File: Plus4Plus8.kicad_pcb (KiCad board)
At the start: 2 copper layers, 22 parts, among them CN1 JOY1, CN2 JOY2, CN3 JOY3, CN4 JOY4, CN5 JOY5, CN6 JOY6, CN7 JOY7, CN8 JOY8, CN9 PLUS4_USERPORT, U1 CD4051B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

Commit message: Initial layout
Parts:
- moved CN1 54.4 mm to (130.9, 121.8)
- moved CN2 54.4 mm to (130.6, 88.8)
- moved CN3 54.4 mm to (129.8, 58.3)
- moved CN4 54.4 mm to (143.4, 31.5)
- moved CN5 54.4 mm to (175.0, 31.0)
- moved CN6 54.4 mm to (188.6, 59.2)
- moved CN7 54.4 mm to (188.6, 91.1)
- moved CN9 54.4 mm to (158.2, 149.1)
- moved RN2 54.4 mm to (144.5, 95.9)
- moved RN3 54.4 mm to (144.1, 66.8)
- moved RN6 54.4 mm to (175.1, 65.9)
- moved U1 54.4 mm to (150.9, 59.9)
- moved U2 54.4 mm to (150.6, 79.0)
- moved U4 54.4 mm to (151.3, 113.7)
- moved U5 54.4 mm to (150.6, 130.7)
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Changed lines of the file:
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@@
   )
   (module Plus4Plus8:DB_9M (layer F.Cu)
-    (at 86.995 89.789 270)
+    (at 130.937 121.793 270)
     (descr "D-SUB 9 pin plug, Tyco P/N 4-338168-2")
     (fp_text reference CN1 (at 0 -2.7 90) (layer F.SilkS)
@@
   )
   (module Plus4Plus8:DB_9M (layer F.Cu)
-    (at 86.614 56.769 270)
+    (at 130.556 88.773 270)
     (descr "D-SUB 9 pin plug, Tyco P/N 4-338168-2")
     (fp_text reference CN2 (at 0 -2.7 90) (layer F.SilkS)
@@
   )
   (module Plus4Plus8:DB_9M (layer F.Cu)
-    (at 85.852 26.289 270)
+    (at 129.794 58.293 270)
     (descr "D-SUB 9 pin plug, Tyco P/N 4-338168-2")
     (fp_text reference CN3 (at 0 -2.7 90) (layer F.SilkS)
@@
   )
   (module Plus4Plus8:DB_9M (layer F.Cu)
-    (at 99.441 -0.508 180)
+    (at 143.383 31.496 180)
     (descr "D-SUB 9 pin plug, Tyco P/N 4-338168-2")
     (fp_text reference CN4 (at 0 -2.7) (layer F.SilkS)
@@
   )
   (module Plus4Plus8:DB_9M (layer F.Cu)
-    (at 131.064 -1.016 180)
+    (at 175.006 30.988 180)
     (descr "D-SUB 9 pin plug, Tyco P/N 4-338168-2")
     (fp_text reference CN5 (at 0 -2.7) (layer F.SilkS)
@@
   )
   (module Plus4Plus8:DB_9M (layer F.Cu)
-    (at 144.653 27.178 90)
+    (at 188.595 59.182 90)
     (descr "D-SUB 9 pin plug, Tyco P/N 4-338168-2")
     (fp_text reference CN6 (at 0 -2.7 90) (layer F.SilkS)
@@
   )
   (module Plus4Plus8:DB_9M (layer F.Cu)
-    (at 144.653 59.055 90)
+    (at 188.595 91.059 90)
     (descr "D-SUB 9 pin plug, Tyco P/N 4-338168-2")
     (fp_text reference CN7 (at 0 -2.7 90) (layer F.SilkS)
@@
   )
   (module Plus4Plus8:DB_9M (layer F.Cu)
-    (at 144.145 91.948 90)
+    (at 188.087 123.952 90)
     (descr "D-SUB 9 pin plug, Tyco P/N 4-338168-2")
     (fp_text reference CN8 (at 0 -2.7 90) (layer F.SilkS)
@@
   )
   (module Plus4Plus8:PLUS4_USERPORT (layer F.Cu)
-    (at 114.3 117.094)
+    (at 158.242 149.098)
     (attr smd)
     (fp_text reference CN9 (at 25.74 -2) (layer F.SilkS)
@@
   )
   (module Resistor_THT:R_Array_SIP6 (layer F.Cu)
-    (at 100.711 95.758 90)
+    (at 144.653 127.762 90)
     (descr "6-pin Resistor SIP pack")
     (tags R)
@@
   )
   (module Resistor_THT:R_Array_SIP6 (layer F.Cu)
-    (at 100.584 63.881 90)
+    (at 144.526 95.885 90)
     (descr "6-pin Resistor SIP pack")
     (tags R)
@@
   )
   (module Resistor_THT:R_Array_SIP6 (layer F.Cu)
-    (at 100.203 34.798 90)
+    (at 144.145 66.802 90)
     (descr "6-pin Resistor SIP pack")
     (tags R)
@@
   )
   (module Resistor_THT:R_Array_SIP6 (layer F.Cu)
-    (at 111.633 12.192 180)
+    (at 155.575 44.196 180)
     (descr "6-pin Resistor SIP pack")
     (tags R)
@@
   )
   (module Resistor_THT:R_Array_SIP6 (layer F.Cu)
-    (at 131.318 12.065 180)
+    (at 175.26 44.069 180)
     (descr "6-pin Resistor SIP pack")
     (tags R)
@@
   )
   (module Resistor_THT:R_Array_SIP6 (layer F.Cu)
-    (at 131.191 33.909 90)
+    (at 175.133 65.913 90)
     (descr "6-pin Resistor SIP pack")
     (tags R)
@@
   )
   (module Resistor_THT:R_Array_SIP6 (layer F.Cu)
-    (at 130.937 65.024 90)
+    (at 174.879 97.028 90)
     (descr "6-pin Resistor SIP pack")
     (tags R)
@@
   )
   (module Resistor_THT:R_Array_SIP6 (layer F.Cu)
-    (at 130.556 98.171 90)
+    (at 174.498 130.175 90)
     (descr "6-pin Resistor SIP pack")
     (tags R)
@@
   )
   (module Package_DIP:DIP-16_W7.62mm_LongPads (layer F.Cu)
-    (at 106.934 27.94 90)
+    (at 150.876 59.944 90)
     (descr "16-lead though-hole mounted DIP package, row spacing 7.62 mm (300 mils), LongPads")
     (tags "THT DIP DIL PDIP 2.54mm 7.62mm 300mil LongPads")
@@
   )
   (module Package_DIP:DIP-16_W7.62mm_LongPads (layer F.Cu)
-    (at 106.68 46.99 90)
+    (at 150.622 78.994 90)
     (descr "16-lead though-hole mounted DIP package, row spacing 7.62 mm (300 mils), LongPads")
     (tags "THT DIP DIL PDIP 2.54mm 7.62mm 300mil LongPads")
@@
   )
   (module Package_DIP:DIP-16_W7.62mm_LongPads (layer F.Cu)
-    (at 107.188 64.643 90)
+    (at 151.13 96.647 90)
     (descr "16-lead though-hole mounted DIP package, row spacing 7.62 mm (300 mils), LongPads")
     (tags "THT DIP DIL PDIP 2.54mm 7.62mm 300mil LongPads")
@@
   )
   (module Package_DIP:DIP-16_W7.62mm_LongPads (layer F.Cu)
-    (at 107.315 81.661 90)
+    (at 151.257 113.665 90)
     (descr "16-lead though-hole mounted DIP package, row spacing 7.62 mm (300 mils), LongPads")
     (tags "THT DIP DIL PDIP 2.54mm 7.62mm 300mil LongPads")
@@
   )
   (module Package_DIP:DIP-16_W7.62mm_LongPads (layer F.Cu)
-    (at 106.68 98.679 90)
+    (at 150.622 130.683 90)
     (descr "16-lead though-hole mounted DIP package, row spacing 7.62 mm (300 mils), LongPads")
     (tags "THT DIP DIL PDIP 2.54mm 7.62mm 300mil LongPads")

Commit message: New layout, way funnier
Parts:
- CN1, CN2, CN3, CN4, CN5, CN6, CN7, CN8: footprint Plus4Plus8:DB_9M -> Connector_Dsub:DSUB-9_Male_EdgeMount_P2.77mm
- CN9: value PLUS4_USERPORT -> DB15F; footprint Plus4Plus8:PLUS4_USERPORT -> Connector_Dsub:DSUB-15_Female_EdgeMount_P2.77mm
- U1, U2, U3, U4, U5: footprint Package_DIP:DIP-16_W7.62mm_LongPads -> Package_DIP:DIP-16_W7.62mm_Socket_LongPads
- moved U1 111.8 mm to (262.6, 61.6)
- moved U2 111.8 mm to (262.4, 80.6)
- moved U3 111.8 mm to (262.9, 98.3)
- moved U4 111.8 mm to (263.0, 115.3)
- moved U5 111.8 mm to (262.4, 132.3)
- moved RN3 29.1 mm to (118.9, 81.1), turned to 60 degrees
- moved RN4 27.9 mm to (134.3, 62.3), turned to 19.9 degrees
- moved RN2 27.1 mm to (118.9, 104.6), turned to 99.9 degrees
- moved CN5 25.7 mm to (165.2, 54.8), turned to 160.1 degrees
- moved CN4 24.0 mm to (137.5, 54.7), turned to 199.9 degrees
- moved CN2 22.1 mm to (111.4, 99.9), turned to 279.9 degrees
- moved CN3 19.6 mm to (116.3, 72.6), turned to 240 degrees
- moved RN5 19.5 mm to (168.4, 62.4), turned to 160.1 degrees
- moved RN6 17.8 mm to (183.4, 81.7), turned to 120 degrees
- moved CN9 17.1 mm to (151.4, 133.5)
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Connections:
- CN9 pad 1: GND -> +5V
- CN9 pad 10: (no net) -> /d4
- CN9 pad 11: (no net) -> /d5
- CN9 pad 12: GND -> /d6
- CN9 pad 2: +5V -> /d0
- CN9 pad 3: (no net) -> /d1
- CN9 pad 6: /d4 -> (no net)
- CN9 pad 7: /d5 -> (no net)
- CN9 pad 8: (no net) -> GND
- CN9 pad 9: (no net) -> +5V
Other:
- board outline added: 89.2 x 87.9 mm

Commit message: Routing in progress
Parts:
- added C1: 100n, Capacitor_THT:C_Disc_D7.0mm_W2.5mm_P5.00mm, F.Cu at (126.0, 76.1)
- added C2: 100n, Capacitor_THT:C_Disc_D7.0mm_W2.5mm_P5.00mm, F.Cu at (151.4, 76.1)
- added C3: 100n, Capacitor_THT:C_Disc_D7.0mm_W2.5mm_P5.00mm, F.Cu at (126.0, 95.4)
- added C4: 100n, Capacitor_THT:C_Disc_D7.0mm_W2.5mm_P5.00mm, F.Cu at (151.4, 95.4)
- added C5: 100n, Capacitor_THT:C_Disc_D7.0mm_W2.5mm_P5.00mm, F.Cu at (138.7, 114.7)
- added C6: 100u, Capacitor_THT:CP_Radial_D6.3mm_P2.50mm, F.Cu at (161.1, 127.4)
- moved U1 134.5 mm to (129.8, 82.4)
- moved U3 133.1 mm to (129.8, 101.7)
- moved U5 120.4 mm to (142.5, 121.0)
- moved U4 108.7 mm to (155.2, 101.7)
- moved U2 107.2 mm to (155.2, 82.4)
- moved RN8 0.92 mm to (169.7, 123.7)
- moved RN1 0.68 mm to (133.0, 123.6)
- moved RN6 0.57 mm to (183.9, 81.4)
- moved RN4 0.47 mm to (133.9, 62.5)
- moved RN2 0.46 mm to (118.5, 104.9)
- moved RN3 0.42 mm to (118.5, 81.0)
- moved RN7 0.40 mm to (184.1, 105.0)
- moved RN5 0.13 mm to (168.5, 62.4)
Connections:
- RN1 pad 2: Net-(CN1-Pad1) -> Net-(CN1-Pad6)
- RN1 pad 3: Net-(CN1-Pad2) -> Net-(CN1-Pad4)
- RN1 pad 5: Net-(CN1-Pad4) -> Net-(CN1-Pad2)
- RN1 pad 6: Net-(CN1-Pad6) -> Net-(CN1-Pad1)
- RN2 pad 2: Net-(CN2-Pad1) -> Net-(CN2-Pad6)
- RN2 pad 3: Net-(CN2-Pad2) -> Net-(CN2-Pad4)
- RN2 pad 5: Net-(CN2-Pad4) -> Net-(CN2-Pad2)
- RN2 pad 6: Net-(CN2-Pad6) -> Net-(CN2-Pad1)
- RN3 pad 2: Net-(CN3-Pad1) -> Net-(CN3-Pad6)
- RN3 pad 3: Net-(CN3-Pad2) -> Net-(CN3-Pad4)
- RN3 pad 5: Net-(CN3-Pad4) -> Net-(CN3-Pad2)
- RN3 pad 6: Net-(CN3-Pad6) -> Net-(CN3-Pad1)
- RN4 pad 2: Net-(CN4-Pad1) -> Net-(CN4-Pad6)
- RN4 pad 3: Net-(CN4-Pad2) -> Net-(CN4-Pad4)
- RN4 pad 5: Net-(CN4-Pad4) -> Net-(CN4-Pad2)
- RN4 pad 6: Net-(CN4-Pad6) -> Net-(CN4-Pad1)
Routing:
- net /d7: track 0.00 -> 121.3 mm
- net /d5: track 0.00 -> 119.2 mm, vias 0 -> 2
- net /d6: track 0.00 -> 109.2 mm, vias 0 -> 3
- net Net-(CN1-Pad2): track 0.00 -> 84.0 mm, vias 0 -> 1
- net +5V: track 0.00 -> 71.2 mm
- net /d0: track 0.00 -> 70.6 mm, vias 0 -> 3
- net Net-(CN4-Pad6): track 0.00 -> 69.7 mm
- net Net-(CN2-Pad2): track 0.00 -> 69.3 mm, vias 0 -> 1
- net Net-(CN3-Pad6): track 0.00 -> 66.1 mm, vias 0 -> 1
- net Net-(CN3-Pad4): track 0.00 -> 62.2 mm, vias 0 -> 1
- net Net-(CN1-Pad4): track 0.00 -> 60.4 mm, vias 0 -> 1
- net Net-(CN4-Pad4): track 0.00 -> 60.0 mm, vias 0 -> 2
- net Net-(CN1-Pad1): track 0.00 -> 58.4 mm, vias 0 -> 3
- net Net-(CN4-Pad3): track 0.00 -> 54.5 mm, vias 0 -> 2
- net /d1: track 0.00 -> 54.5 mm, vias 0 -> 1
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
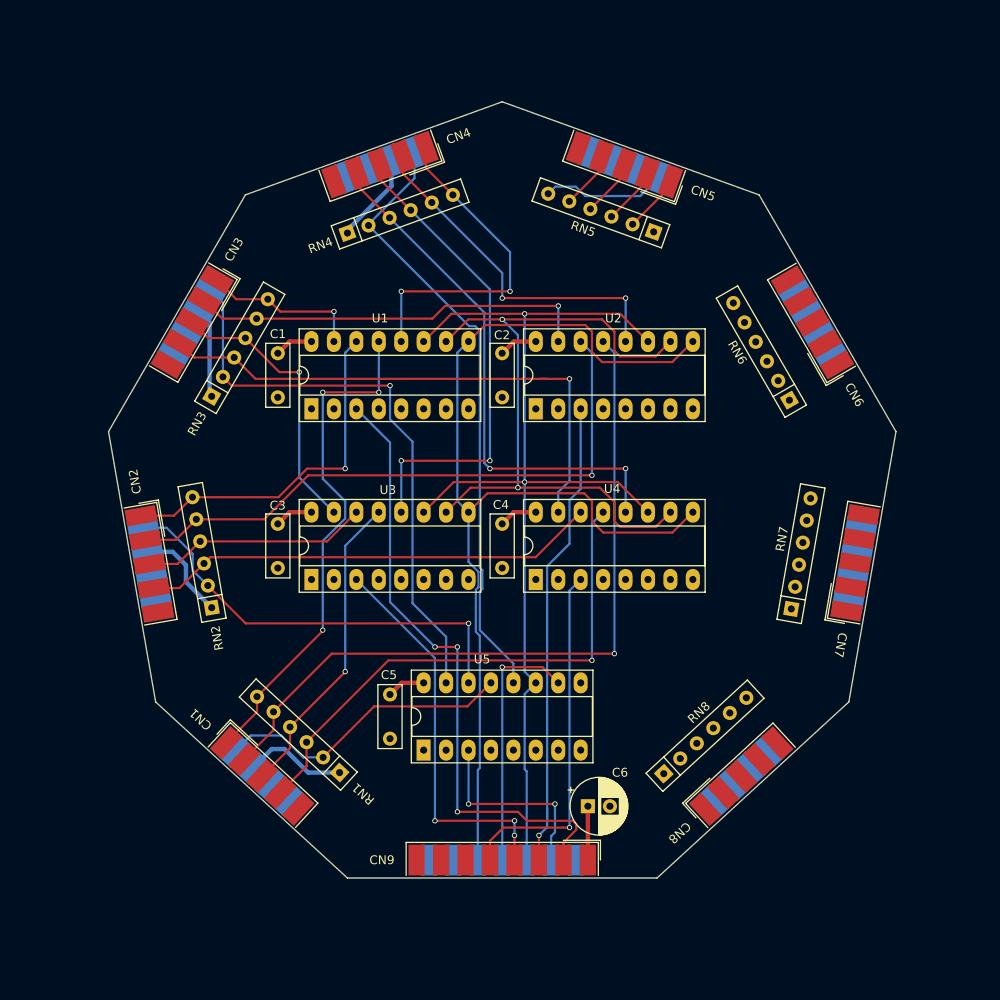
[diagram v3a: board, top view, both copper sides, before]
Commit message: Rough routing done except power
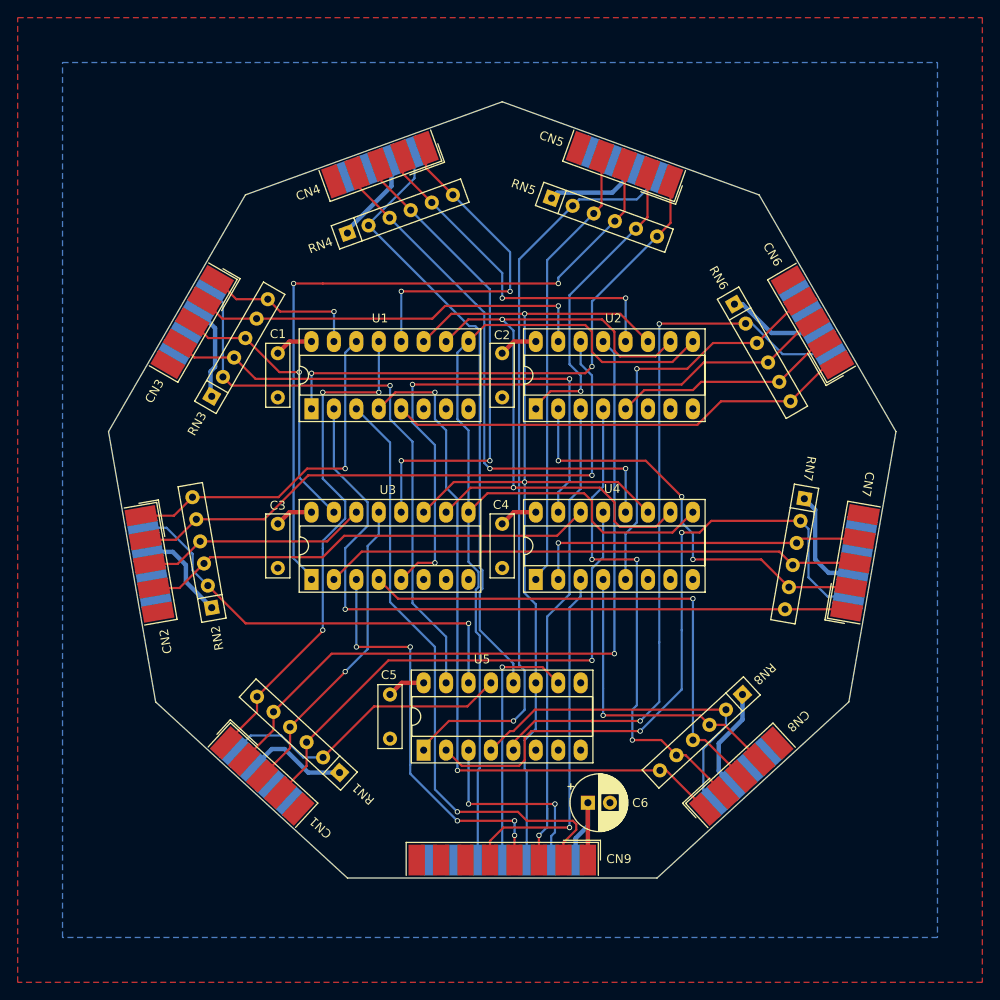
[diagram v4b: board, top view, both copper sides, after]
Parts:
- moved RN8 12.6 mm to (178.6, 114.7), turned to 222.6 degrees
- moved RN7 12.6 mm to (185.6, 92.6), turned to 260.1 degrees
- moved RN6 12.5 mm to (177.7, 70.5), turned to 300 degrees
- moved RN5 12.2 mm to (157.0, 58.5), turned to 340.1 degrees
- moved C6 0.40 mm to (161.1, 127.0)
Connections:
- RN5 pad 2: Net-(CN5-Pad1) -> Net-(CN5-Pad6)
- RN5 pad 3: Net-(CN5-Pad2) -> Net-(CN5-Pad4)
- RN5 pad 5: Net-(CN5-Pad4) -> Net-(CN5-Pad2)
- RN5 pad 6: Net-(CN5-Pad6) -> Net-(CN5-Pad1)
- RN6 pad 2: Net-(CN6-Pad1) -> Net-(CN6-Pad6)
- RN6 pad 3: Net-(CN6-Pad2) -> Net-(CN6-Pad4)
- RN6 pad 5: Net-(CN6-Pad4) -> Net-(CN6-Pad2)
- RN6 pad 6: Net-(CN6-Pad6) -> Net-(CN6-Pad1)
- RN7 pad 2: Net-(CN7-Pad1) -> Net-(CN7-Pad6)
- RN7 pad 3: Net-(CN7-Pad2) -> Net-(CN7-Pad4)
- RN7 pad 5: Net-(CN7-Pad4) -> Net-(CN7-Pad2)
- RN7 pad 6: Net-(CN7-Pad6) -> Net-(CN7-Pad1)
- RN8 pad 2: Net-(CN8-Pad1) -> Net-(CN8-Pad6)
- RN8 pad 3: Net-(CN8-Pad2) -> Net-(CN8-Pad4)
- RN8 pad 5: Net-(CN8-Pad4) -> Net-(CN8-Pad2)
- RN8 pad 6: Net-(CN8-Pad6) -> Net-(CN8-Pad1)
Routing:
- net Net-(CN6-Pad6): track 0.00 -> 83.0 mm, vias 0 -> 2
- net Net-(CN7-Pad1): track 0.00 -> 82.1 mm, vias 0 -> 1
- net Net-(CN8-Pad1): track 0.00 -> 80.9 mm, vias 0 -> 2
- net Net-(CN7-Pad6): track 0.00 -> 76.6 mm, vias 0 -> 2
- net Net-(CN5-Pad3): track 6.61 -> 80.9 mm, vias 0 -> 2
- net Net-(CN6-Pad3): track 0.00 -> 74.1 mm, vias 0 -> 2
- net Net-(CN5-Pad6): track 14.2 -> 84.5 mm, vias 0 -> 1
- net Net-(CN7-Pad3): track 0.00 -> 61.0 mm
- net Net-(CN8-Pad3): track 0.00 -> 59.6 mm, vias 0 -> 1
- net Net-(CN8-Pad2): track 0.00 -> 56.1 mm, vias 0 -> 3
- net Net-(CN5-Pad1): track 6.63 -> 60.7 mm, vias 0 -> 2
- net +5V: track 71.2 -> 125.2 mm
- net Net-(CN6-Pad1): track 0.00 -> 52.9 mm
- net Net-(CN7-Pad2): track 0.00 -> 48.4 mm, vias 0 -> 3
- net Net-(CN6-Pad4): track 0.00 -> 46.1 mm, vias 0 -> 1
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- added copper zone on B.Cu, net GND
- added copper zone on F.Cu, net GND

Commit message: Working on ground plane Top half TBD
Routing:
- net +5V: track 125.2 -> 326.8 mm, vias 0 -> 1
- net /d6: track 109.0 -> 131.4 mm, vias 3 -> 2
- net Net-(CN4-Pad6): track 69.7 -> 86.8 mm, vias 0 -> 2
- net /d5: track 119.2 -> 130.1 mm, vias 2 -> 1
- net Net-(CN8-Pad3): track 59.6 -> 68.7 mm
- net Net-(CN2-Pad6): track 49.2 -> 57.6 mm
- net Net-(CN6-Pad4): track 46.1 -> 51.0 mm
- net Net-(CN1-Pad1): track 58.4 -> 63.2 mm
- net /d2: track 46.6 -> 42.3 mm, vias 5 -> 1
- net Net-(CN3-Pad6): track 66.1 -> 69.2 mm
- net Net-(CN7-Pad3): track 61.0 -> 64.1 mm
- net Net-(CN8-Pad2): track 56.1 -> 59.2 mm
- net /d0: track 69.1 -> 66.3 mm
- net Net-(CN7-Pad1): track 82.1 -> 79.8 mm
- net Net-(CN1-Pad6): track 34.2 -> 36.6 mm
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
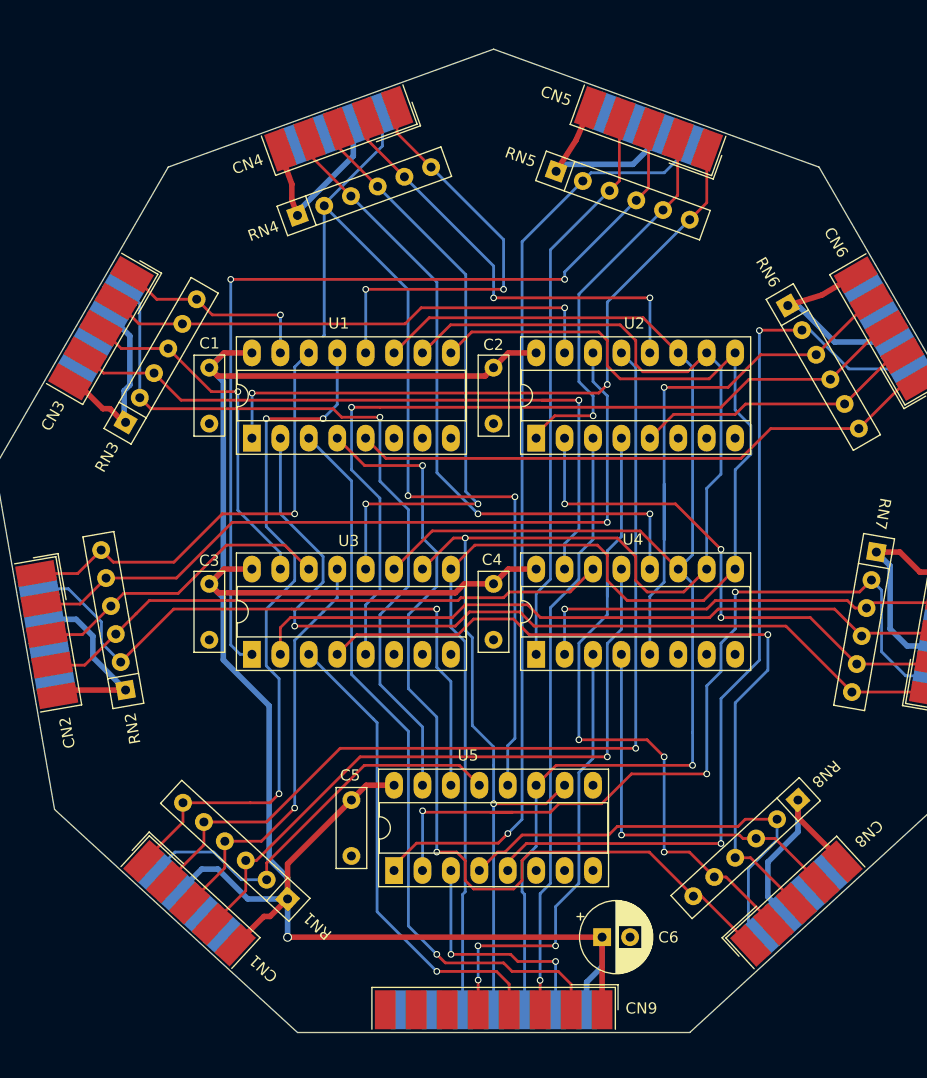
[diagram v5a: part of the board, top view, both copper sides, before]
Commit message: Top ground plane almost done
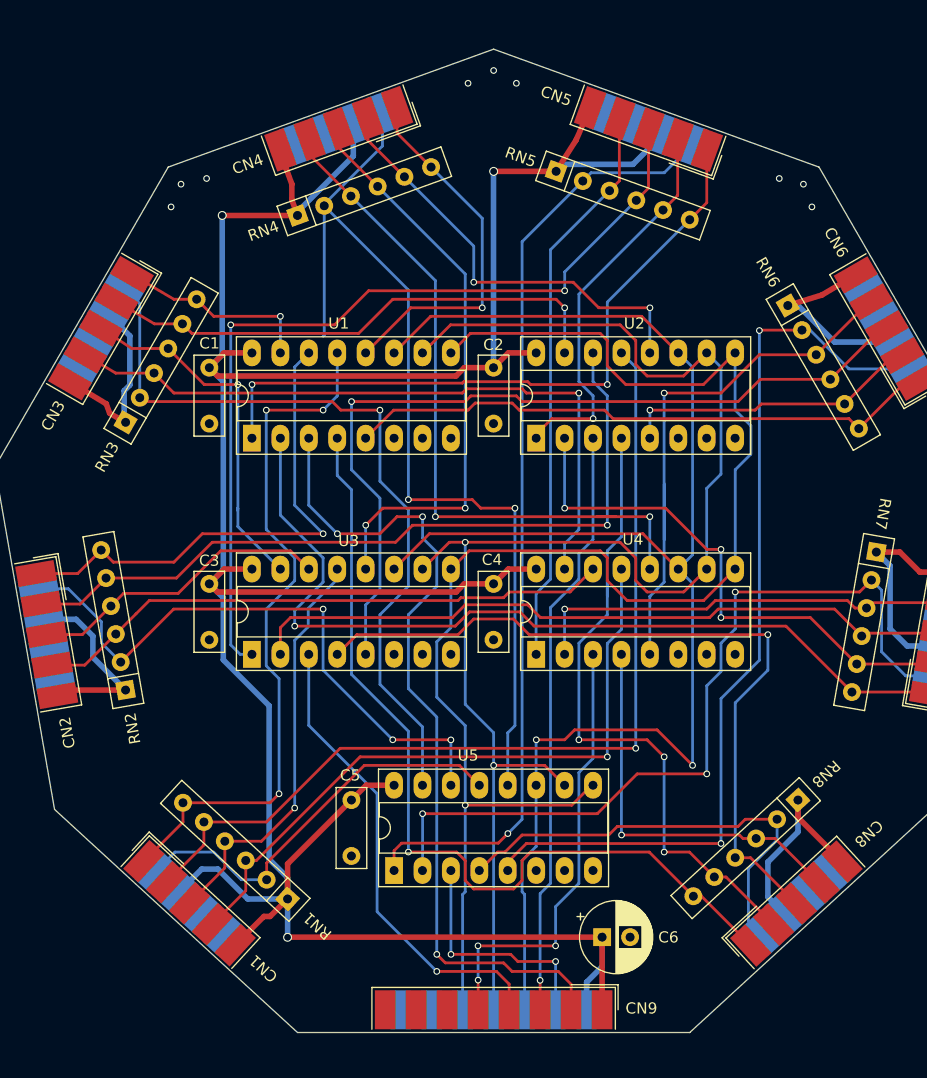
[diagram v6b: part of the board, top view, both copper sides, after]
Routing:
- net +5V: track 326.8 -> 368.9 mm, vias 1 -> 3
- net /d7: track 121.6 -> 134.5 mm, vias 0 -> 1
- net /d0: track 66.3 -> 75.0 mm, vias 1 -> 3
- net Net-(CN4-Pad1): track 38.2 -> 33.1 mm, vias 2 -> 1
- net /d5: track 130.1 -> 135.0 mm, vias 1 -> 2
- net Net-(CN2-Pad1): track 41.1 -> 45.8 mm
- net Net-(CN4-Pad4): track 60.0 -> 63.9 mm
- net Net-(CN8-Pad1): track 82.2 -> 78.5 mm, vias 2 -> 1
- net Net-(CN2-Pad6): track 57.6 -> 54.7 mm, vias 1 -> 3
- net Net-(CN4-Pad3): track 54.5 -> 52.0 mm
- net Net-(CN7-Pad6): track 76.4 -> 74.2 mm
- net Net-(CN5-Pad3): track 81.3 -> 79.5 mm
- net Net-(CN6-Pad2): track 25.6 -> 27.1 mm, vias 0 -> 1
- net Net-(CN3-Pad2): track 45.5 -> 46.6 mm
- net Net-(CN5-Pad6): track 84.0 -> 84.8 mm
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
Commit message: 0 unrouted! But some space for improvements left
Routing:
- net +5V: track 368.9 -> 475.0 mm, vias 3 -> 9
- net Net-(CN3-Pad3): track 32.4 -> 34.2 mm
- net Net-(CN6-Pad6): track 82.7 -> 81.0 mm
- net Net-(CN5-Pad1): track 61.4 -> 59.9 mm
- net Net-(CN8-Pad3): track 68.7 -> 67.4 mm
- net GND: vias 9 -> 12
